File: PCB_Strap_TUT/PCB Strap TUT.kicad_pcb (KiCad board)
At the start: 2 copper layers, 40.6 x 40.6 mm, 45 parts, among them J1 Debug, Q1 Q_PMOS_GDS, SW1 SW_SPST, U1 PIC16F1503-ISL

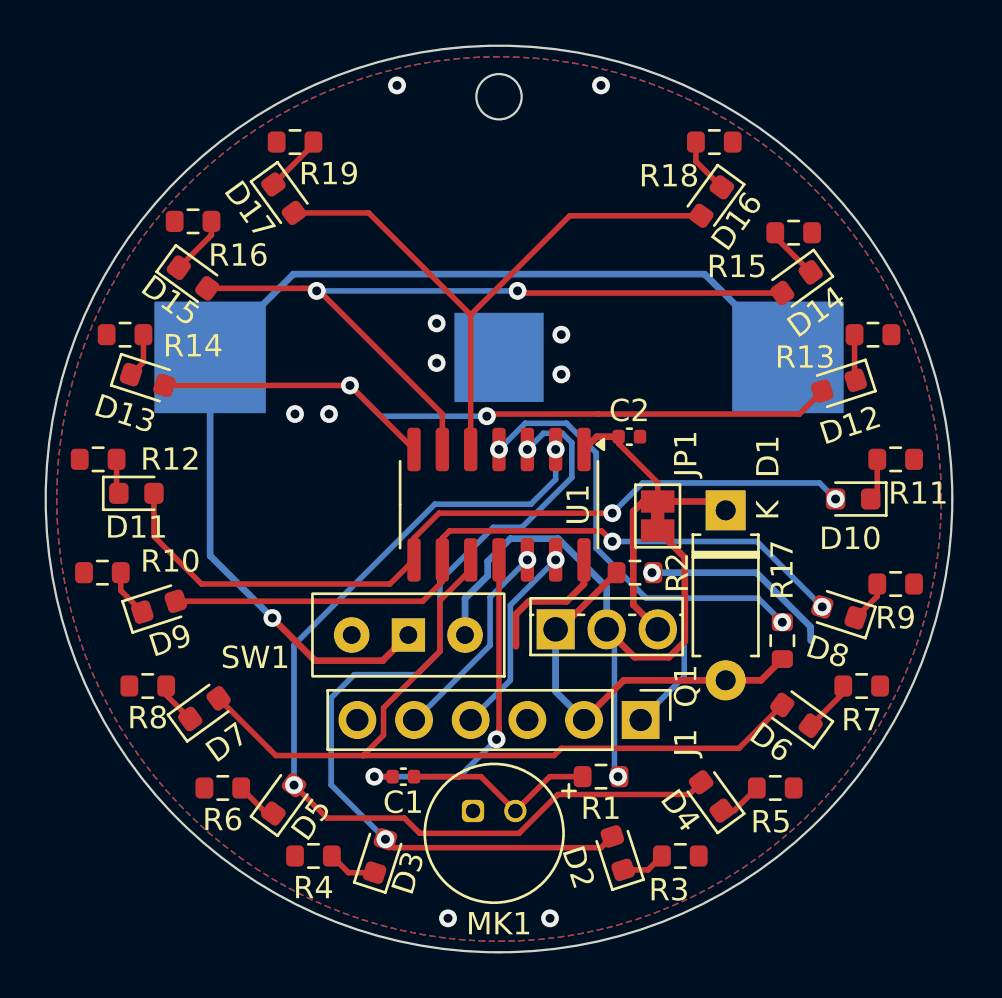
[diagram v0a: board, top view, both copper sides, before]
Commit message: adjust some silk  and add EasyEDA Files
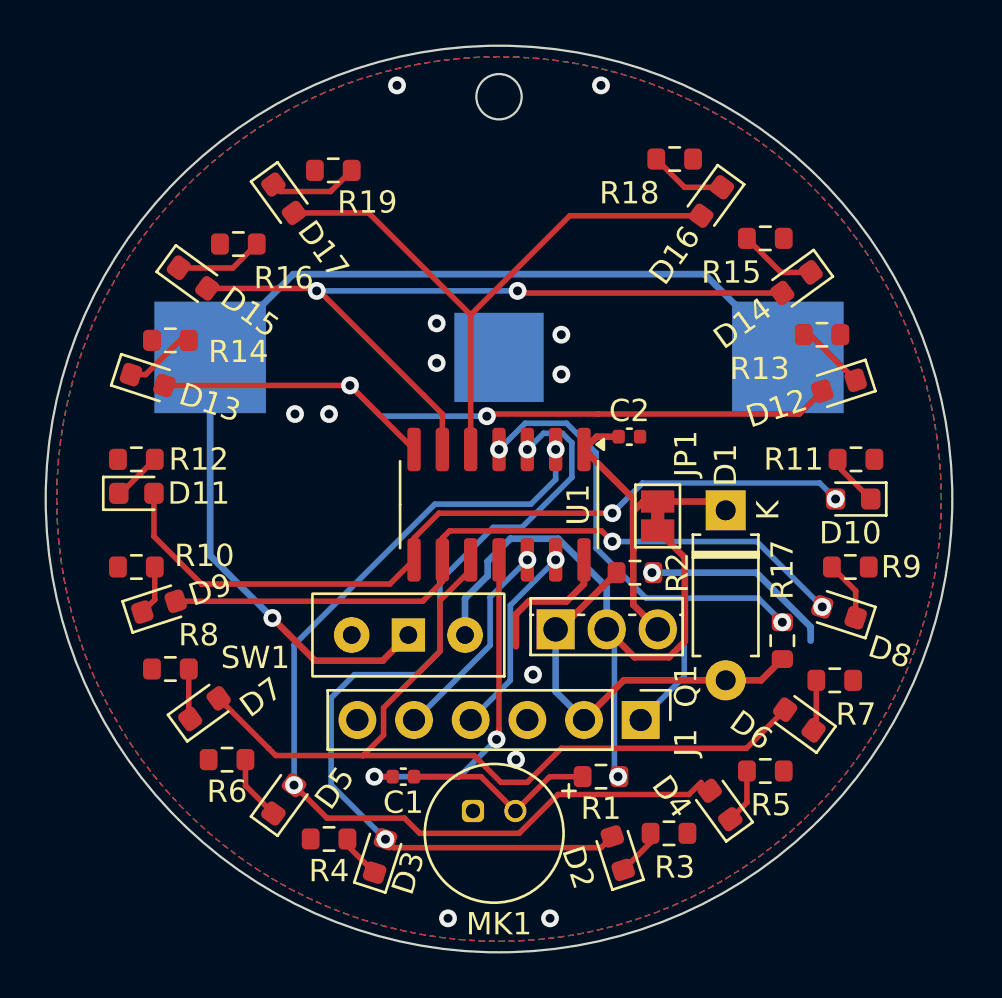
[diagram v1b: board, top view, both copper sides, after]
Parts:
- moved R13 2.29 mm to (141.5, 87.9)
- moved R16 2.27 mm to (115.3, 83.8)
- moved R9 2.17 mm to (142.7, 98.3)
- moved R19 2.13 mm to (119.6, 80.5)
- moved R14 2.05 mm to (112.3, 88.1)
- moved R18 1.93 mm to (134.9, 80.0)
- moved R11 1.78 mm to (143.0, 93.5)
- moved R12 1.72 mm to (110.7, 93.5)
- moved R10 1.55 mm to (110.7, 98.3)
- moved R15 1.30 mm to (138.9, 83.6)
- moved R6 1.28 mm to (114.8, 106.9)
- moved R8 1.27 mm to (112.3, 102.9)
- moved R7 1.23 mm to (142.0, 103.4)
- moved R3 1.14 mm to (134.6, 110.2)
- moved R4 1.03 mm to (119.4, 110.5)
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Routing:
- net Net-(D17-K): track 2.65 -> 4.03 mm
- net Net-(D15-K): track 2.68 -> 3.94 mm
- net Net-(D13-K): track 2.02 -> 3.23 mm
- net Net-(D12-K): track 2.06 -> 3.18 mm
- net Net-(D14-K): track 2.44 -> 3.49 mm
- net /RC0: track 38.0 -> 39.1 mm
- net Net-(D5-K): track 1.92 -> 2.93 mm
- net Net-(D16-K): track 2.51 -> 3.46 mm
- net Net-(D10-K): track 1.90 -> 2.81 mm
- net Net-(D11-K): track 1.57 -> 2.39 mm
- net Net-(D8-K): track 1.91 -> 2.72 mm
- net GND: vias 11 -> 13
